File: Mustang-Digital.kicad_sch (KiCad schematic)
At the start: 0 parts

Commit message: 3D models.
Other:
- sheet Left Side Analog renamed Analog Interface
- removed sheet Right Side Analog
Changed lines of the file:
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@@
 			(color 67 255 69 1.0000)
 		)
-		(property "Sheetname" "Left Side Analog"
+		(property "Sheetname" "Analog Interface"
 			(at 43.18 31.6226 0)
 			(show_name yes)
@@
 				)
 			)
-		)
-	)
-	(sheet
-		(at 144.78 33.02)
-		(size 95.25 87.63)
-		(fields_autoplaced yes)
-		(stroke
-			(width 0.254)
-			(type solid)
-			(color 43 77 255 1)
-		)
-		(fill
-			(color 255 42 46 1.0000)
-		)
-		(property "Sheetname" "Right Side Analog"
-			(at 144.78 31.6226 0)
-			(show_name yes)
-			(effects
-				(font
-					(size 2.54 2.54)
-					(bold yes)
-				)
-				(justify left bottom)
-			)
-		)
-		(property "Sheetfile" "RSA.kicad_sch"
-			(at 144.78 121.2854 0)
-			(show_name yes)
-			(effects
-				(font
-					(size 1.27 1.27)
-					(bold yes)
-				)
-				(justify left top)
-			)
-		)
-		(instances
-			(project "Mustang-Digital"
-				(path "/5e27fdeb-580f-476f-92aa-43cee2f9d9cd"
-					(page "3")
-				)
-			)

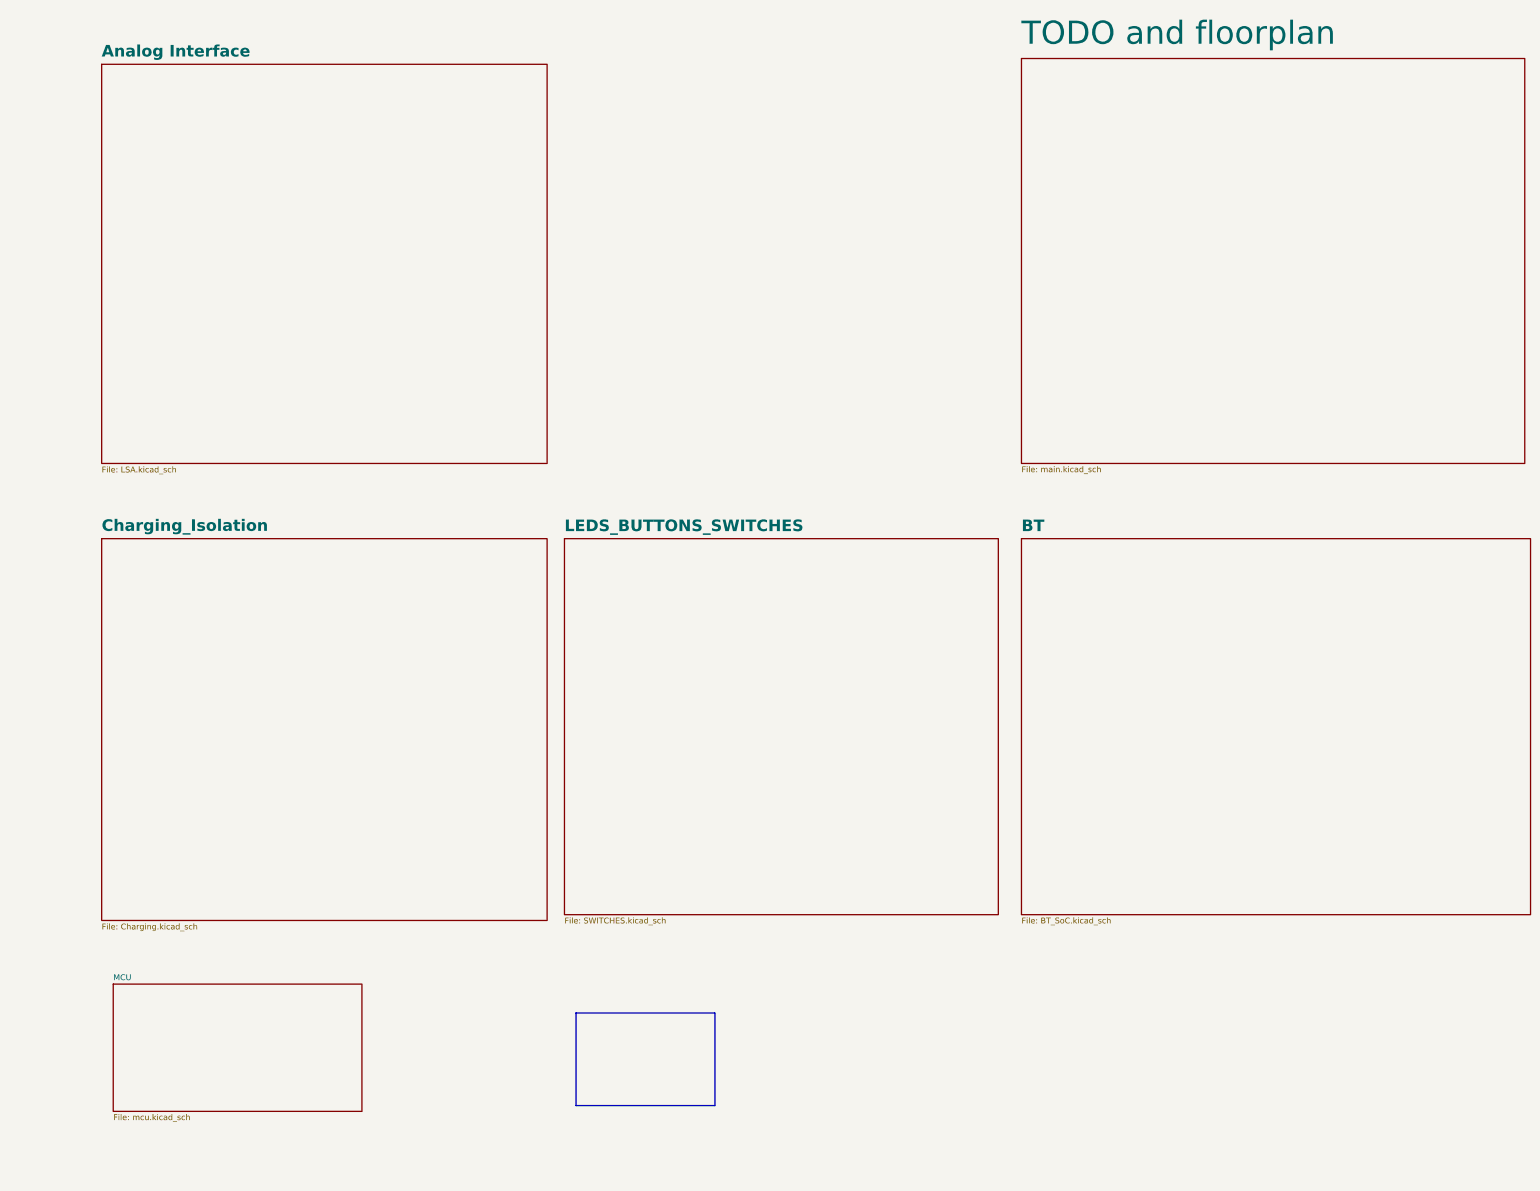
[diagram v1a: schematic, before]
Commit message: Electrical Rules Check fixes in progress.
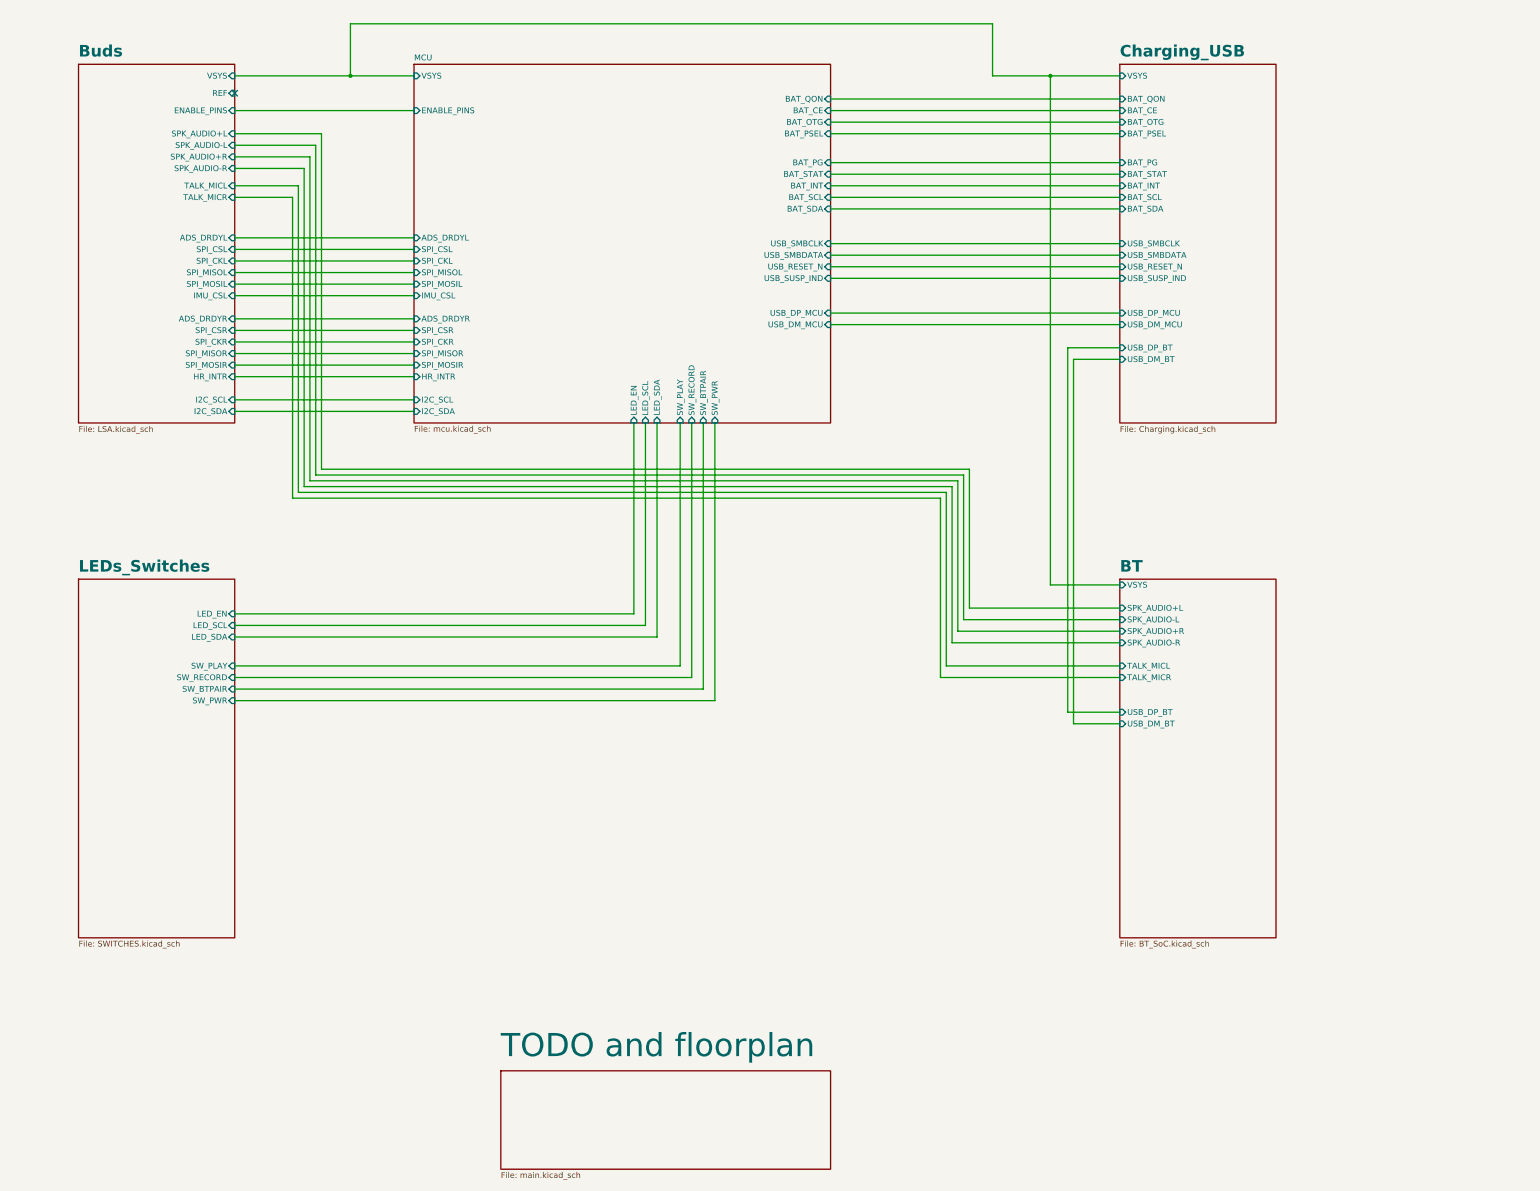
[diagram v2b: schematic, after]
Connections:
- no-connect marks 0 -> 1
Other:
- sheet Analog Interface renamed Buds
- sheet Charging_Isolation renamed Charging_USB
- sheet LEDS_BUTTONS_SWITCHES renamed LEDs_Switches
- sheet BT ports: added SPK_AUDIO+L, SPK_AUDIO+R, SPK_AUDIO-L, SPK_AUDIO-R, TALK_MICL, TALK_MICR, USB_DM_BT, USB_DP_BT, VSYS; removed none
- sheet Buds ports: added ADS_DRDYL, ADS_DRDYR, ENABLE_PINS, HR_INTR, I2C_SCL, I2C_SDA, IMU_CSL, REF, SPI_CKL, SPI_CKR, SPI_CSL, SPI_CSR, SPI_MISOL, SPI_MISOR, SPI_MOSIL, SPI_MOSIR, SPK_AUDIO+L, SPK_AUDIO+R, SPK_AUDIO-L, SPK_AUDIO-R, TALK_MICL, TALK_MICR, VSYS; removed none
- sheet Charging_USB ports: added BAT_CE, BAT_INT, BAT_OTG, BAT_PG, BAT_PSEL, BAT_QON, BAT_SCL, BAT_SDA, BAT_STAT, USB_DM_BT, USB_DM_MCU, USB_DP_BT, USB_DP_MCU, USB_RESET_N, USB_SMBCLK, USB_SMBDATA, USB_SUSP_IND, VSYS; removed none
- sheet LEDs_Switches ports: added LED_EN, LED_SCL, LED_SDA, SW_BTPAIR, SW_PLAY, SW_PWR, SW_RECORD; removed none
- sheet MCU ports: added ADS_DRDYL, ADS_DRDYR, BAT_CE, BAT_INT, BAT_OTG, BAT_PG, BAT_PSEL, BAT_QON, BAT_SCL, BAT_SDA, BAT_STAT, ENABLE_PINS, HR_INTR, I2C_SCL, I2C_SDA, IMU_CSL, LED_EN, LED_SCL, LED_SDA, SPI_CKL, SPI_CKR, SPI_CSL, SPI_CSR, SPI_MISOL, SPI_MISOR, SPI_MOSIL, SPI_MOSIR, SW_BTPAIR, SW_PLAY, SW_PWR, SW_RECORD, USB_DM_MCU, USB_DP_MCU, USB_RESET_N, USB_SMBCLK, USB_SMBDATA, USB_SUSP_IND, VSYS; removed none

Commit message: wip
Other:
- sheet BT ports: added AIL, AIR, DMIC_CLK, DMIC_L, DMIC_R, HPL+, HPL-, HPR+, HPR-, I2S_DR, I2S_DT, I2S_MCLK, I2S_RFS, I2S_SCLK, LDO_EN, MIC1+, MIC1-, MIC2+, MICBIAS, MIN2-, P0_1, P0_2, P0_3, P0_5, P0_6, P0_7, P2_3, P2_6, P2_7, P3_2, PWM, PWR_MFB, RST_N, SCL_TDI, SDA_TCK, TEMP_AUX, TEMP_BATT, UART_CTS, UART_RTS, UART_RXD, UART_TXD, UART_TX_IND, USB_DM, USB_DP, VBATT, VUSB; removed SPK_AUDIO+L, SPK_AUDIO+R, SPK_AUDIO-L, SPK_AUDIO-R, TALK_MICL, TALK_MICR, USB_DM_BT, USB_DP_BT

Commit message: wip
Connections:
- no-connect marks 1 -> 24
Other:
- sheet Charging_USB ports: added VBATT, VUSB; removed none
- sheet MCU ports: added BUD_ADS_DRDYL, BUD_ADS_DRDYR, BUD_ENABLE_PINS, BUD_HR_INTR, BUD_I2C_SCL, BUD_I2C_SDA, BUD_IMU_CSL, BUD_SPI_CKL, BUD_SPI_CKR, BUD_SPI_CSL, BUD_SPI_CSR, BUD_SPI_MISOL, BUD_SPI_MISOR, BUD_SPI_MOSIL, BUD_SPI_MOSIR, USB_DM, USB_DP; removed ADS_DRDYL, ADS_DRDYR, ENABLE_PINS, HR_INTR, I2C_SCL, I2C_SDA, IMU_CSL, SPI_CKL, SPI_CKR, SPI_CSL, SPI_CSR, SPI_MISOL, SPI_MISOR, SPI_MOSIL, SPI_MOSIR, USB_DM_MCU, USB_DP_MCU

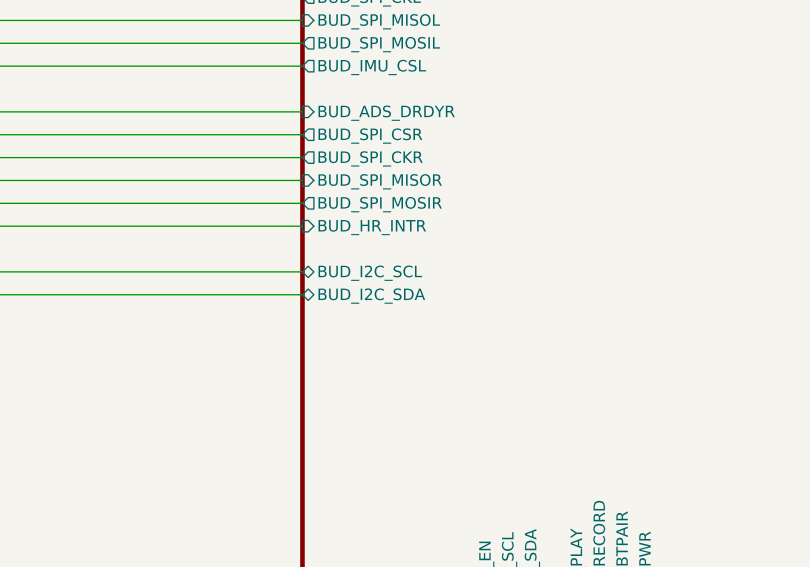
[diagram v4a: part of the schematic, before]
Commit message: Use all YAGEO 0603 resistors.
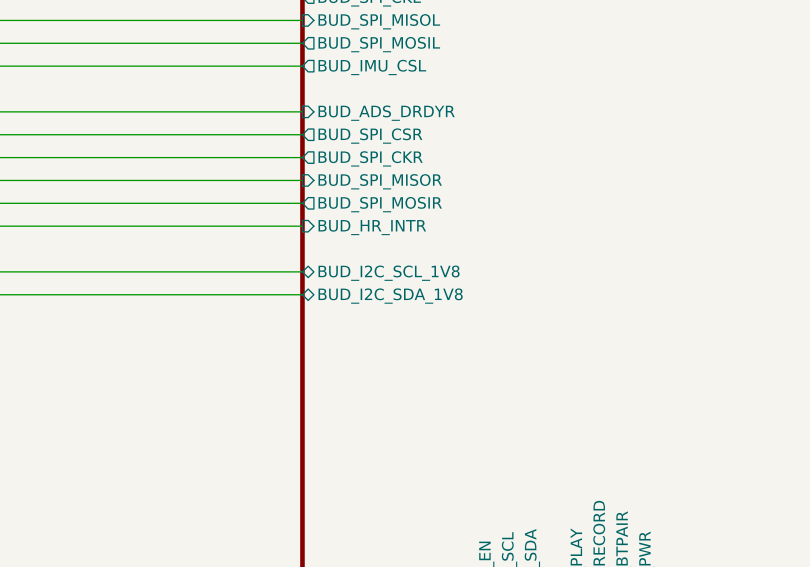
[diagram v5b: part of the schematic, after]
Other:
- sheet MCU ports: added BUD_I2C_SCL_1V8, BUD_I2C_SDA_1V8; removed BUD_I2C_SCL, BUD_I2C_SDA
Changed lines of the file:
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@@
 			)
 		)
-		(pin "BUD_I2C_SDA" bidirectional
+		(pin "BUD_I2C_SDA_1V8" bidirectional
 			(at 111.76 109.22 180)
 			(effects
@@
 			)
 		)
-		(pin "BUD_I2C_SCL" bidirectional
+		(pin "BUD_I2C_SCL_1V8" bidirectional
 			(at 111.76 106.68 180)
 			(effects
